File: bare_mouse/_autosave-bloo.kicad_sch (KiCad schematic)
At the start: 103 parts, among them J1 Serial Debug Header, J10 Conn_01x06_Female, J2 SWD Header, J4 Conn_ARM_JTAG_SWD_10, J5 SWD Header, M1 M1_Conn_Alt, M2 M2_Conn_Alt, Q0 TEFT4300, Q1 TEFT4300, Q10 Q_NMOS_GSD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

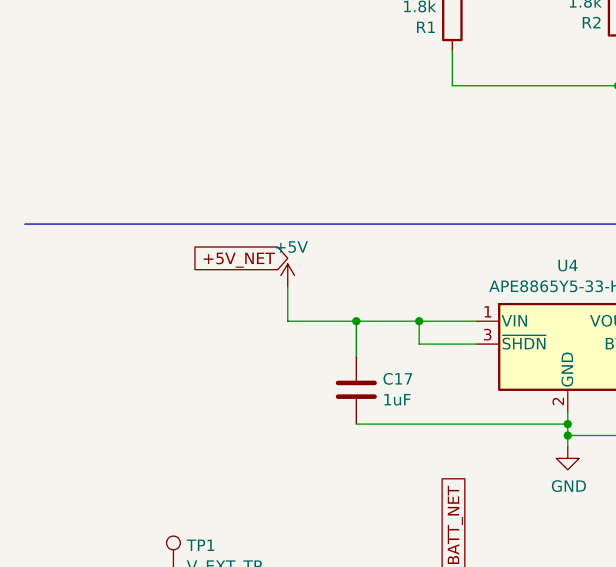
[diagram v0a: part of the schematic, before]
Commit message: power module
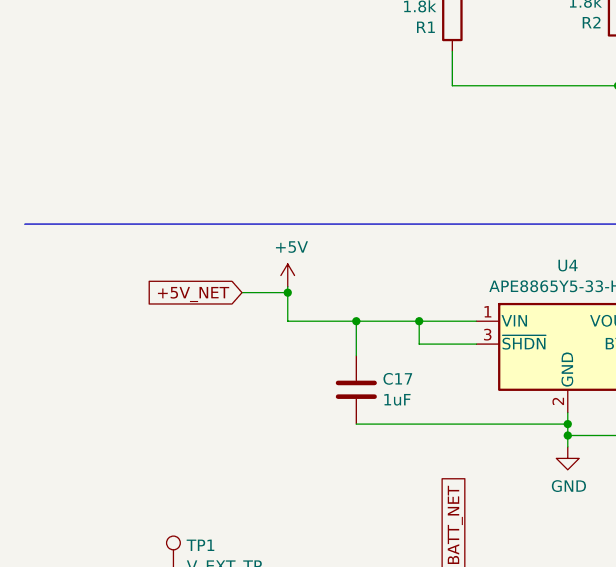
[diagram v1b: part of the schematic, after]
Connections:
- net +5V_NET is gone; now on net +5V: C10.1, C13.1, C16.1, TP3.1, U3.2 (VO), U5.3 (*CE), U6.1 (VIN)
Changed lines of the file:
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@@
 	)
 	(junction
+		(at 41.91 133.35)
+		(diameter 0)
+		(color 0 0 0 0)
+	)
+	(junction
 		(at 150.495 97.79)
 		(diameter 0)
@@
 	(wire
 		(pts
+			(xy 41.91 133.35) (xy 41.91 132.715)
+		)
+		(stroke
+			(width 0)
+			(type default)
+		)
+	)
+	(wire
+		(pts
 			(xy 259.715 169.545) (xy 233.045 169.545)
 		)
@@
 	(wire
 		(pts
-			(xy 41.91 136.525) (xy 41.91 132.715)
+			(xy 36.83 133.35) (xy 41.91 133.35)
+		)
+		(stroke
+			(width 0)
+			(type default)
+		)
+	)
+	(wire
+		(pts
+			(xy 41.91 136.525) (xy 41.91 133.35)
 		)
 		(stroke
@@
 	(global_label "+5V_NET"
 		(shape input)
-		(at 41.91 129.54 180)
+		(at 36.83 133.35 180)
 		(fields_autoplaced yes)
 		(effects
@@
 		)
 		(property "Intersheetrefs" "${INTERSHEET_REFS}"
-			(at 31.2938 129.54 0)
+			(at 26.2138 133.35 0)
 			(effects
 				(font
